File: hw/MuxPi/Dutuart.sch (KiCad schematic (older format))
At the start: 14 parts, among them P4 T821108A1S100CEU, U2 MCP6002-E/SN, U5 SN74LVC2T45DCTT, U6 SN74LVC2T45DCTT

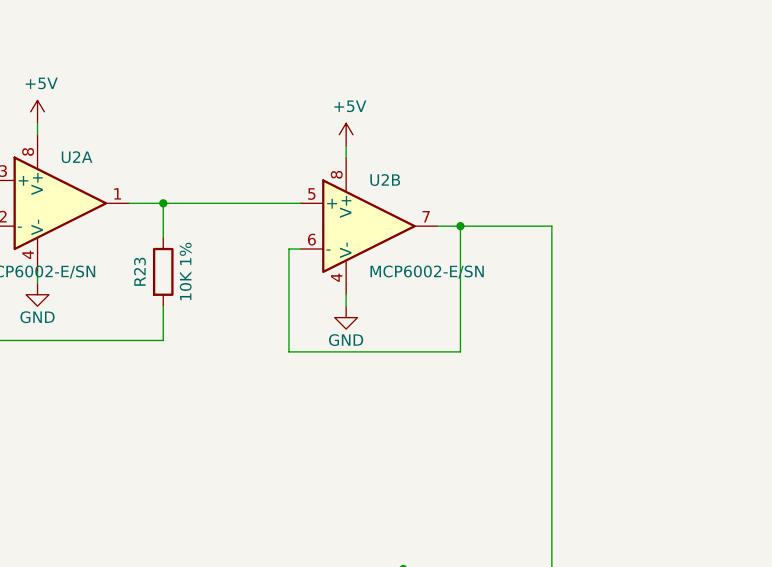
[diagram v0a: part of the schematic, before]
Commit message: Add detailed info to MuxPi electronic components
The additional information includes manufacturer names and
manufacturer symbols for all components except ceramic capacitors
and resistors. It allows to create BOM (Bill Of Materials) with
actual product names.

Change-Id: Id1c518bba60322d4b8b132ad14261806070abc27
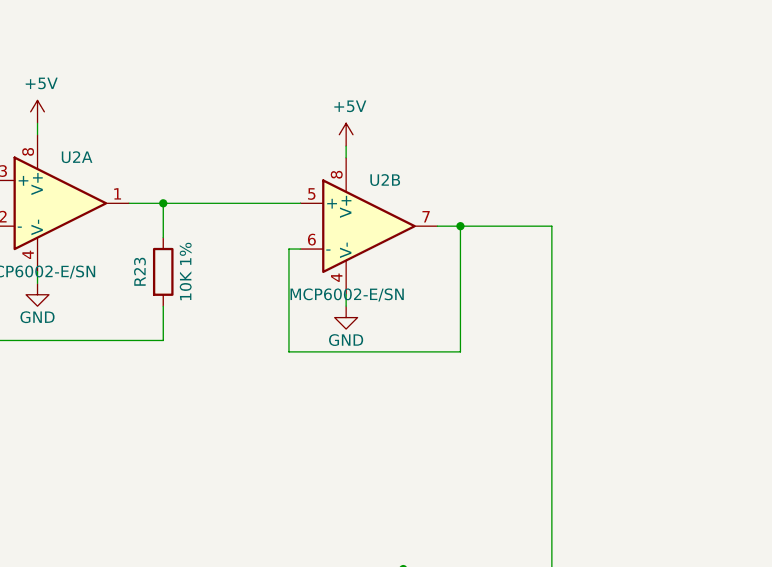
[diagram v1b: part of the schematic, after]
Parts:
- D9: Manufacturer (none) -> KINGBRIGHT ELECTRONIC; Symbol (none) -> KPT-2012SGC
- P4: Manufacturer (none) -> CONNFLY; Symbol (none) -> DS1021-2*4SF1-1
- U2: Manufacturer (none) -> MICROCHIP TECHNOLOGY; Symbol (none) -> MCP6002-E/SN
- U5, U6: Manufacturer (none) -> TEXAS INSTRUMENTS; Symbol (none) -> SN74LVC2T45DCTT
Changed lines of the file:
@@
 F 3 "http://www.tme.eu/pl/Document/6c30e63cb6e35247759643c975f2fb23/SN74LVC2T45DCTT.pdf" H 4150 3800 50  0001 C CNN
 F 4 "http://www.tme.eu/pl/details/sn74lvc2t45dctt/konwertery-logiczne/texas-instruments/" H 4250 3800 60  0001 C CNN "Shop link"
+F 5 "TEXAS INSTRUMENTS" H 4250 3800 50  0001 C CNN "Manufacturer"
+F 6 "SN74LVC2T45DCTT" H 4250 3800 50  0001 C CNN "Symbol"
 	1    4250 3800
 	1    0    0    -1
@@
 F 3 "http://www.tme.eu/pl/Document/cda30bae7de800ca9be388e3f3476120/T821-1-08-S1.pdf" H 5450 3000 60  0001 C CNN
 F 4 "http://www.tme.eu/pl/details/t821-1-08-s1/zlacza-idc/amphenol/t821108a1s100ceu/" H 5450 4200 60  0001 C CNN "Shop link"
+F 5 "CONNFLY" H 5450 4200 50  0001 C CNN "Manufacturer"
+F 6 "DS1021-2*4SF1-1" H 5450 4200 50  0001 C CNN "Symbol"
 	1    5450 4200
 	1    0    0    -1
@@
 $EndComp
 $Comp
-L MuxPi:SN74LVC2T45 U6
-U 1 1 584E7273
-P 4250 4650
-F 0 "U6" H 4250 4950 50  0000 C CNN
-F 1 "SN74LVC2T45DCTT" H 4250 4350 50  0000 C CNN
-F 2 "mux-footprints:SSOP-8" H 4150 4650 50  0001 C CIN
-F 3 "http://www.tme.eu/pl/Document/6c30e63cb6e35247759643c975f2fb23/SN74LVC2T45DCTT.pdf" H 4150 4650 50  0001 C CNN
-F 4 "http://www.tme.eu/pl/details/sn74lvc2t45dctt/konwertery-logiczne/texas-instruments/" H 4250 4650 60  0001 C CNN "Shop link"
-	1    4250 4650
-	1    0    0    -1
-$EndComp
-$Comp
-L MuxPi:LED_ALT D9
-U 1 1 58D934D3
-P 4850 5200
-F 0 "D9" V 4888 5082 50  0000 R CNN
-F 1 "KPT-2012SGC (GREEN)" V 4797 5082 50  0000 R CNN
-F 2 "Diodes_SMD:D_0805" H 4850 5200 50  0001 C CNN
-F 3 "http://www.tme.eu/pl/Document/0a4307e0e1e070f4f6d553134056548e/kpt-2012.pdf" H 4850 5200 50  0001 C CNN
-F 4 "http://www.tme.eu/pl/details/kpt-2012sgc/diody-led-smd-kolorowe/kingbright-electronic/" V 4850 5200 60  0001 C CNN "Shop link"
-	1    4850 5200
-	0    -1   -1   0
-$EndComp
-$Comp
 L MuxPi:R R6
 U 1 1 58D93B8B
@@
 F 3 "http://www.tme.eu/pl/Document/c98656c49a036767b89c9bb93e3dda4a/mcp6001_2_4.pdf" H 4250 1800 50  0001 C CNN
 F 4 "http://www.tme.eu/pl/details/mcp6002-e_sn/wzmacniacze-operacyjne-smd/microchip-technology/" H 4250 1650 60  0001 C CNN "Shop link"
+F 5 "MICROCHIP TECHNOLOGY" H 4250 1650 50  0001 C CNN "Manufacturer"
+F 6 "MCP6002-E/SN" H 4250 1650 50  0001 C CNN "Symbol"
 	1    4250 1650
-	1    0    0    -1
-$EndComp
-$Comp
-L MuxPi:MCP6002 U2
-U 2 1 58E19358
-P 5600 1750
-F 0 "U2" H 5600 1950 50  0000 L CNN
-F 1 "MCP6002-E/SN" H 5600 1550 50  0000 L CNN
-F 2 "mux-footprints:SOIC-8" H 5500 1800 50  0001 C CNN
-F 3 "http://www.tme.eu/pl/Document/c98656c49a036767b89c9bb93e3dda4a/mcp6001_2_4.pdf" H 5600 1900 50  0001 C CNN
-F 4 "http://www.tme.eu/pl/details/mcp6002-e_sn/wzmacniacze-operacyjne-smd/microchip-technology/" H 5600 1750 60  0001 C CNN "Shop link"
-	2    5600 1750
 	1    0    0    -1
 $EndComp
@@
 Wire Wire Line
 	5750 3250 6250 3250
+$Comp
+L MuxPi:MCP6002 U2
+U 2 1 5A886D70
+P 5600 1750
+F 0 "U2" H 5600 1950 50  0000 L CNN
+F 1 "MCP6002-E/SN" H 5250 1450 50  0000 L CNN
+F 2 "mux-footprints:SOIC-8" H 5500 1800 50  0001 C CNN
+F 3 "http://www.tme.eu/pl/Document/c98656c49a036767b89c9bb93e3dda4a/mcp6001_2_4.pdf" H 5600 1900 50  0001 C CNN
+F 4 "http://www.tme.eu/pl/details/mcp6002-e_sn/wzmacniacze-operacyjne-smd/microchip-technology/" H 5600 1750 60  0001 C CNN "Shop link"
+F 5 "MICROCHIP TECHNOLOGY" H 5600 1750 50  0001 C CNN "Manufacturer"
+F 6 "MCP6002-E/SN" H 5600 1750 50  0001 C CNN "Symbol"
+	2    5600 1750
+	1    0    0    -1
+$EndComp
+$Comp
+L MuxPi:LED_ALT D9
+U 1 1 5A887879
+P 4850 5200
+F 0 "D9" V 4888 5082 50  0000 R CNN
+F 1 "KPT-2012SGC (GREEN)" V 4797 5082 50  0000 R CNN
+F 2 "Diodes_SMD:D_0805" H 4850 5200 50  0001 C CNN
+F 3 "http://www.tme.eu/pl/Document/0a4307e0e1e070f4f6d553134056548e/kpt-2012.pdf" H 4850 5200 50  0001 C CNN
+F 4 "http://www.tme.eu/pl/details/kpt-2012sgc/diody-led-smd-kolorowe/kingbright-electronic/" V 4850 5200 60  0001 C CNN "Shop link"
+F 5 "KINGBRIGHT ELECTRONIC" V 4850 5200 50  0001 C CNN "Manufacturer"
+F 6 "KPT-2012SGC" V 4850 5200 50  0001 C CNN "Symbol"
+	1    4850 5200
+	0    -1   -1   0
+$EndComp
+$Comp
+L MuxPi:SN74LVC2T45 U6
+U 1 1 5A88984D
+P 4250 4650
+F 0 "U6" H 4250 4950 50  0000 C CNN
+F 1 "SN74LVC2T45DCTT" H 4250 4350 50  0000 C CNN
+F 2 "mux-footprints:SSOP-8" H 4150 4650 50  0001 C CIN
+F 3 "http://www.tme.eu/pl/Document/6c30e63cb6e35247759643c975f2fb23/SN74LVC2T45DCTT.pdf" H 4150 4650 50  0001 C CNN
+F 4 "http://www.tme.eu/pl/details/sn74lvc2t45dctt/konwertery-logiczne/texas-instruments/" H 4250 4650 60  0001 C CNN "Shop link"
+F 5 "TEXAS INSTRUMENTS" H 4250 4650 50  0001 C CNN "Manufacturer"
+F 6 "SN74LVC2T45DCTT" H 4250 4650 50  0001 C CNN "Symbol"
+	1    4250 4650
+	1    0    0    -1
+$EndComp
 $EndSCHEMATC
